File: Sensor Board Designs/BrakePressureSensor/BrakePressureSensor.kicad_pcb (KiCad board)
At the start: 2 copper layers, 50.8 x 25.4 mm, 18 parts, among them J1 ICSP, J2 POWER/CAN, J3 Conn_01x04, U1 ATtiny841-SS, U2 MCP25625-x-SS, U3 74HC04

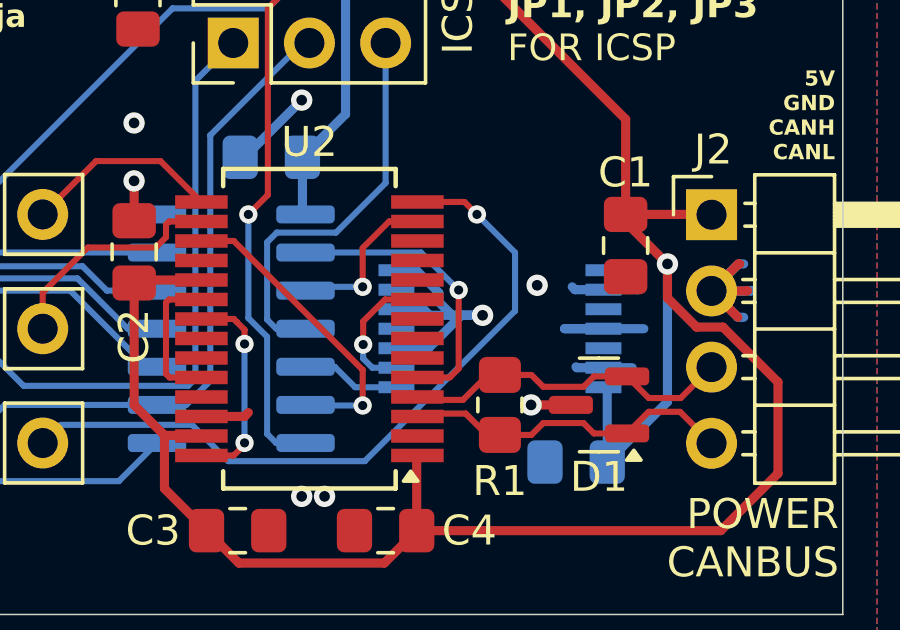
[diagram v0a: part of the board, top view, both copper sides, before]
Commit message: Fixed grounds
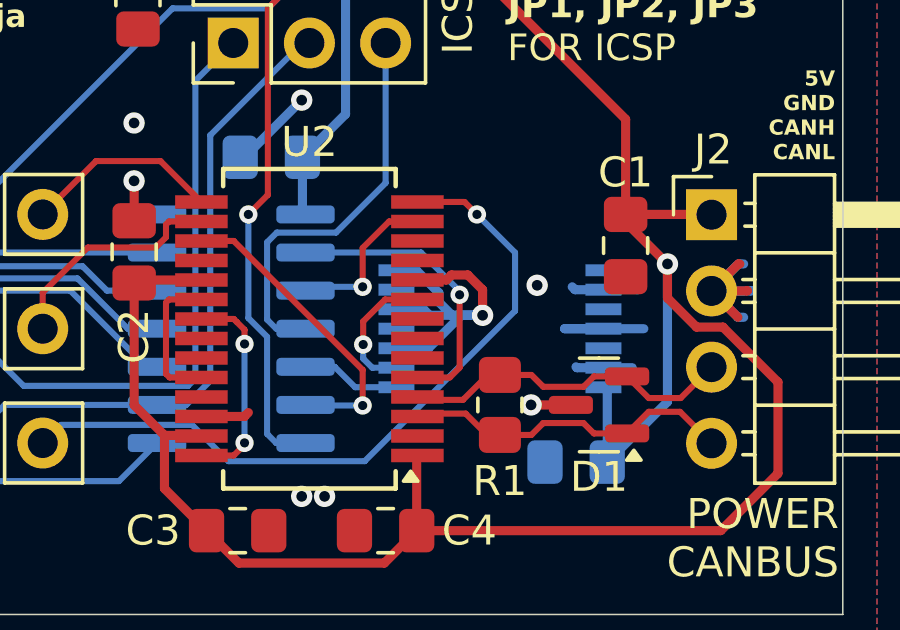
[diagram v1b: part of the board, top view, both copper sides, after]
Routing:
- net GND: track 33.2 -> 36.5 mm
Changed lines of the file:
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@@
+	)
+	(segment
+		(start 147.571481 103.15)
+		(end 147.738141 102.98334)
+		(width 0.3048)
+		(layer "F.Cu")
+		(net 1)
 	)
 	(segment
@@
 	)
 	(segment
+		(start 147.738141 102.98334)
+		(end 148.285235 102.98334)
+		(width 0.3048)
+		(layer "F.Cu")
+		(net 1)
+	)
+	(segment
 		(start 157.309 102.616)
 		(end 157.353 102.616)
@@
 	)
 	(segment
+		(start 148.777826 103.475931)
+		(end 148.777826 104.327826)
+		(width 0.3048)
+		(layer "F.Cu")
+		(net 1)
+	)
+	(segment
 		(start 156.41 103.515)
 		(end 157.309 102.616)
@@
 	)
 	(segment
+		(start 148.285235 102.98334)
+		(end 148.777826 103.475931)
+		(width 0.3048)
+		(layer "F.Cu")
+		(net 1)
+	)
+	(segment
 		(start 137.163 101.176)
 		(end 137.163 99.8504)
+		(width 0.3048)
+		(layer "F.Cu")
+		(net 1)
+	)
+	(segment
+		(start 146.605 103.15)
+		(end 147.571481 103.15)
 		(width 0.3048)
 		(layer "F.Cu")
@@
 	)
 	(segment
-		(start 147.979911 103.484701)
-		(end 147.979911 106.103289)
-		(width 0.2032)
-		(layer "F.Cu")
-		(net 12)
-	)
-	(segment
 		(start 147.6832 106.4)
 		(end 146.605 106.4)
@@
 	)
 	(segment
-		(start 147.979911 106.103289)
+		(start 148.011688 103.64374)
+		(end 148.011688 106.071512)
+		(width 0.2032)
+		(layer "F.Cu")
+		(net 12)
+	)
+	(segment
+		(start 148.011688 106.071512)
 		(end 147.6832 106.4)
 		(width 0.2032)
@@
 	)
 	(via
-		(at 147.979911 103.484701)
+		(at 148.011688 103.64374)
 		(size 0.6096)
 		(drill 0.3048)
@@
 	)
 	(segment
-		(start 147.979911 103.484701)
-		(end 147.974301 103.484701)
+		(start 148.011688 103.522088)
+		(end 146.7246 102.235)
 		(width 0.2032)
 		(layer "B.Cu")
@@
 	)
 	(segment
-		(start 147.974301 103.484701)
-		(end 146.7246 102.235)
-		(width 0.2032)
-		(layer "B.Cu")
+		(start 148.011688 103.64374)
+		(end 148.011688 103.522088)
+		(width 0.2032)
+		(layer "B.Cu")
